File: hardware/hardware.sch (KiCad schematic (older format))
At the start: 98 parts, among them J1 DB25_Female, J2 USB_B_Micro, J3 RJ45_Bel_SI-60062-F-68net, U1 MIC5319, U11 ENC28J60x-SO, U12 74LVC14, U2 74LVTH126, U3 74LVTH126, U4 LM1117-ADJ, U5 74LVTH126, U6 74LVTH126, U7 STM32F072R8Tx, U8 74LVC245, Y1 8MHz, Y2 25MHz

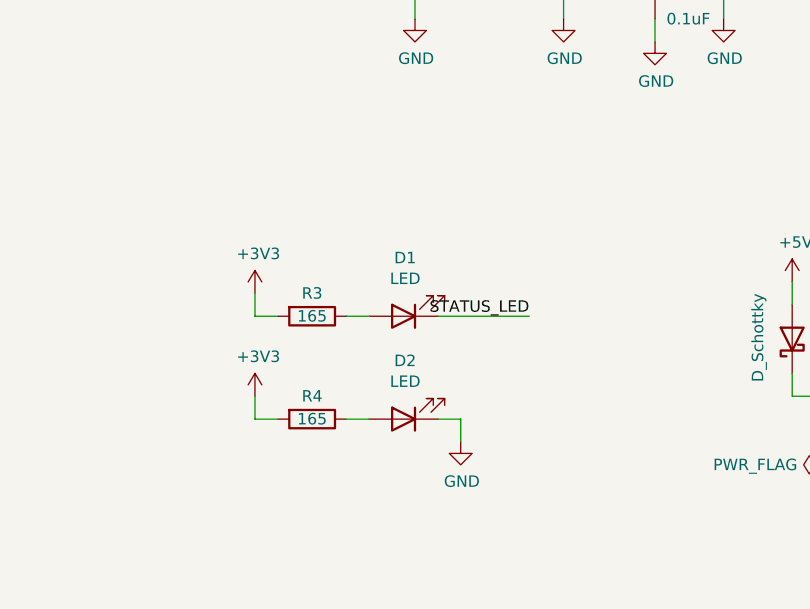
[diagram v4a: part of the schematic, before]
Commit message: feat: add connectors for external LEDs
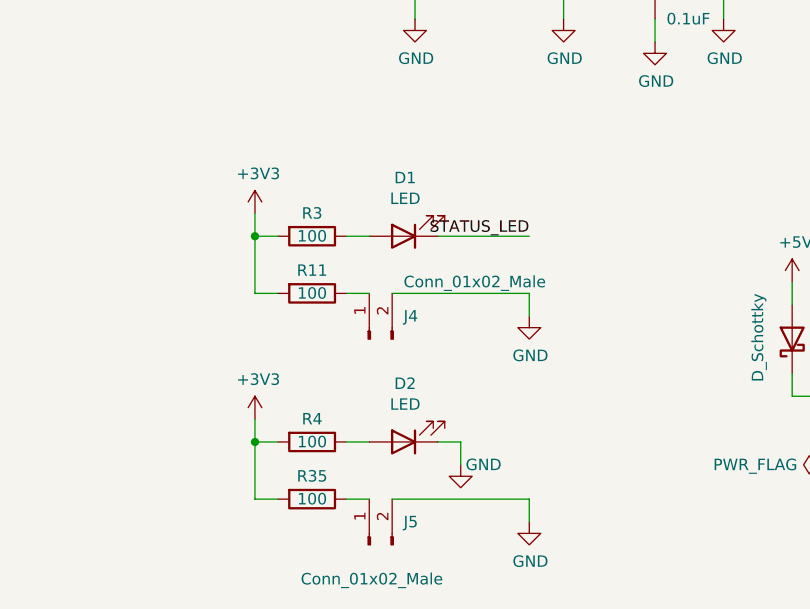
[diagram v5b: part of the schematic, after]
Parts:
- added J4, J5: Conn_01x02_Male, Connector_PinHeader_2.54mm:PinHeader_1x02_P2.54mm_Vertical, symbol Connector:Conn_01x02_Male
- added R11, R35: 100, Resistor_SMD:R_0805_2012Metric_Pad1.15x1.40mm_HandSolder, symbol Device:R
- J1: footprint kicad-footprints-perso:D25S13A -> kicad-footprints-perso:DSUB-25_Female_Horizontal_Double
- R3, R4: value 165 -> 100
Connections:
- net +3V3: now also R11.2, R35.2
- net GND: now also J4.2 (Pin_2), J5.2 (Pin_2)
- new net: J4.1 (Pin_1), R11.1
- new net: J5.1 (Pin_1), R35.1
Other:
- moved on the sheet: D1, D2, R3, R4
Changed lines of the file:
@@
 $EndComp
 Wire Wire Line
-	1000 10250 1000 10350
-Wire Wire Line
-	1000 10350 1100 10350
-Wire Wire Line
-	1400 10350 1500 10350
-Wire Wire Line
-	1800 10350 1900 10350
-Wire Wire Line
-	1900 10350 1900 10450
+	1000 10350 1000 10450
+Wire Wire Line
+	1000 10450 1100 10450
+Wire Wire Line
+	1400 10450 1500 10450
+Wire Wire Line
+	1800 10450 1900 10450
+Wire Wire Line
+	1900 10450 1900 10550
 $Comp
 L power:GND #PWR?
 U 1 1 6030DBBA
-P 1900 10450
-F 0 "#PWR?" H 1900 10200 50  0001 C CNN
-F 1 "GND" H 1905 10277 50  0000 C CNN
-F 2 "" H 1900 10450 50  0001 C CNN
-F 3 "" H 1900 10450 50  0001 C CNN
-	1    1900 10450
-	1    0    0    -1
-$EndComp
-Wire Wire Line
-	1000 9800 1000 9900
-Wire Wire Line
-	1000 9900 1100 9900
+P 1900 10550
+F 0 "#PWR?" H 1900 10300 50  0001 C CNN
+F 1 "GND" H 2000 10550 50  0000 C CNN
+F 2 "" H 1900 10550 50  0001 C CNN
+F 3 "" H 1900 10550 50  0001 C CNN
+	1    1900 10550
+	1    0    0    -1
+$EndComp
+Wire Wire Line
+	1000 9450 1000 9550
+Wire Wire Line
+	1000 9550 1100 9550
 $Comp
 L power:+3V3 #PWR?
 U 1 1 6032DBF1
-P 1000 9800
-F 0 "#PWR?" H 1000 9650 50  0001 C CNN
-F 1 "+3V3" H 1015 9973 50  0000 C CNN
-F 2 "" H 1000 9800 50  0001 C CNN
-F 3 "" H 1000 9800 50  0001 C CNN
-	1    1000 9800
-	1    0    0    -1
-$EndComp
-Wire Wire Line
-	1400 9900 1500 9900
-Wire Wire Line
-	1800 9900 2200 9900
-Text Label 2200 9900 2    50   ~ 0
+P 1000 9450
+F 0 "#PWR?" H 1000 9300 50  0001 C CNN
+F 1 "+3V3" H 1015 9623 50  0000 C CNN
+F 2 "" H 1000 9450 50  0001 C CNN
+F 3 "" H 1000 9450 50  0001 C CNN
+	1    1000 9450
+	1    0    0    -1
+$EndComp
+Wire Wire Line
+	1400 9550 1500 9550
+Wire Wire Line
+	1800 9550 2200 9550
+Text Label 2200 9550 2    50   ~ 0
 STATUS_LED
 NoConn ~ 12300 8400
@@
 L Device:LED D1
 U 1 1 6034F780
-P 1650 9900
-F 0 "D1" H 1643 9645 50  0000 C CNN
-F 1 "LED" H 1643 9736 50  0000 C CNN
-F 2 "LED_SMD:LED_1206_3216Metric_Pad1.42x1.75mm_HandSolder" H 1650 9900 50  0001 C CNN
-F 3 "~" H 1650 9900 50  0001 C CNN
-F 4 "60-1456-1-ND" H 1650 9900 50  0001 C CNN "Digi-Key_PN"
-	1    1650 9900
+P 1650 9550
+F 0 "D1" H 1643 9295 50  0000 C CNN
+F 1 "LED" H 1643 9386 50  0000 C CNN
+F 2 "LED_SMD:LED_1206_3216Metric_Pad1.42x1.75mm_HandSolder" H 1650 9550 50  0001 C CNN
+F 3 "~" H 1650 9550 50  0001 C CNN
+F 4 "60-1456-1-ND" H 1650 9550 50  0001 C CNN "Digi-Key_PN"
+	1    1650 9550
 	-1   0    0    1
 $EndComp
@@
 L Device:R R3
 U 1 1 6032EE5C
-P 1250 9900
-F 0 "R3" V 1150 9900 50  0000 C CNN
-F 1 "165" V 1250 9900 50  0000 C CNN
-F 2 "Resistor_SMD:R_0805_2012Metric_Pad1.15x1.40mm_HandSolder" V 1180 9900 50  0001 C CNN
-F 3 "~" H 1250 9900 50  0001 C CNN
-F 4 "RMCF0805FT165RCT-ND" H 1250 9900 50  0001 C CNN "Digi-Key_PN"
-	1    1250 9900
+P 1250 9550
+F 0 "R3" V 1150 9550 50  0000 C CNN
+F 1 "100" V 1250 9550 50  0000 C CNN
+F 2 "Resistor_SMD:R_0805_2012Metric_Pad1.15x1.40mm_HandSolder" V 1180 9550 50  0001 C CNN
+F 3 "~" H 1250 9550 50  0001 C CNN
+F 4 "RMCF0805FT165RCT-ND" H 1250 9550 50  0001 C CNN "Digi-Key_PN"
+	1    1250 9550
 	0    1    1    0
 $EndComp
@@
 L Device:LED D2
 U 1 1 602EDF34
-P 1650 10350
-F 0 "D2" H 1643 10095 50  0000 C CNN
-F 1 "LED" H 1643 10186 50  0000 C CNN
-F 2 "LED_SMD:LED_1206_3216Metric_Pad1.42x1.75mm_HandSolder" H 1650 10350 50  0001 C CNN
-F 3 "~" H 1650 10350 50  0001 C CNN
-F 4 "60-1456-1-ND" H 1650 10350 50  0001 C CNN "Digi-Key_PN"
-	1    1650 10350
+P 1650 10450
+F 0 "D2" H 1643 10195 50  0000 C CNN
+F 1 "LED" H 1643 10286 50  0000 C CNN
+F 2 "LED_SMD:LED_1206_3216Metric_Pad1.42x1.75mm_HandSolder" H 1650 10450 50  0001 C CNN
+F 3 "~" H 1650 10450 50  0001 C CNN
+F 4 "60-1456-1-ND" H 1650 10450 50  0001 C CNN "Digi-Key_PN"
+	1    1650 10450
 	-1   0    0    1
 $EndComp
@@
 L Device:R R4
 U 1 1 602CE979
-P 1250 10350
-F 0 "R4" V 1150 10350 50  0000 C CNN
-F 1 "165" V 1250 10350 50  0000 C CNN
-F 2 "Resistor_SMD:R_0805_2012Metric_Pad1.15x1.40mm_HandSolder" V 1180 10350 50  0001 C CNN
-F 3 "~" H 1250 10350 50  0001 C CNN
-F 4 "RMCF0805FT165RCT-ND" H 1250 10350 50  0001 C CNN "Digi-Key_PN"
-	1    1250 10350
+P 1250 10450
+F 0 "R4" V 1150 10450 50  0000 C CNN
+F 1 "100" V 1250 10450 50  0000 C CNN
+F 2 "Resistor_SMD:R_0805_2012Metric_Pad1.15x1.40mm_HandSolder" V 1180 10450 50  0001 C CNN
+F 3 "~" H 1250 10450 50  0001 C CNN
+F 4 "RMCF0805FT165RCT-ND" H 1250 10450 50  0001 C CNN "Digi-Key_PN"
+	1    1250 10450
 	0    1    1    0
 $EndComp
@@
 F 0 "J1" H 15430 2096 50  0000 L CNN
 F 1 "DB25_Female" H 15430 2005 50  0000 L CNN
-F 2 "kicad-footprints-perso:D25S13A" H 15250 2050 50  0001 C CNN
+F 2 "kicad-footprints-perso:DSUB-25_Female_Horizontal_Double" H 15250 2050 50  0001 C CNN
 F 3 " ~" H 15250 2050 50  0001 C CNN
 F 4 "609-1507-ND" H 15250 2050 50  0001 C CNN "Digi-Key_PN"
@@
 L power:+3V3 #PWR?
 U 1 1 603F481A
-P 1000 10250
-F 0 "#PWR?" H 1000 10100 50  0001 C CNN
-F 1 "+3V3" H 1015 10423 50  0000 C CNN
-F 2 "" H 1000 10250 50  0001 C CNN
-F 3 "" H 1000 10250 50  0001 C CNN
-	1    1000 10250
+P 1000 10350
+F 0 "#PWR?" H 1000 10200 50  0001 C CNN
+F 1 "+3V3" H 1015 10523 50  0000 C CNN
+F 2 "" H 1000 10350 50  0001 C CNN
+F 3 "" H 1000 10350 50  0001 C CNN
+	1    1000 10350
 	1    0    0    -1
 $EndComp
@@
 	1    0    0    -1
 $EndComp
+Wire Wire Line
+	1000 9800 1100 9800
+Wire Wire Line
+	1400 9800 1500 9800
+$Comp
+L Device:R R11
+U 1 1 6118A7D0
+P 1250 9800
+F 0 "R11" V 1150 9800 50  0000 C CNN
+F 1 "100" V 1250 9800 50  0000 C CNN
+F 2 "Resistor_SMD:R_0805_2012Metric_Pad1.15x1.40mm_HandSolder" V 1180 9800 50  0001 C CNN
+F 3 "~" H 1250 9800 50  0001 C CNN
+F 4 "RMCF0805FT165RCT-ND" H 1250 9800 50  0001 C CNN "Digi-Key_PN"
+	1    1250 9800
+	0    1    1    0
+$EndComp
+Wire Wire Line
+	1000 9550 1000 9800
+Connection ~ 1000 9550
+$Comp
+L Connector:Conn_01x02_Male J4
+U 1 1 61266EA3
+P 1500 10000
+F 0 "J4" V 1600 9850 50  0000 R CNN
+F 1 "Conn_01x02_Male" V 1750 9850 50  0000 R CNN
+F 2 "Connector_PinHeader_2.54mm:PinHeader_1x02_P2.54mm_Vertical" H 1500 10000 50  0001 C CNN
+F 3 "~" H 1500 10000 50  0001 C CNN
+	1    1500 10000
+	0    -1   -1   0
+$EndComp
+Wire Wire Line
+	1600 9800 2200 9800
+Wire Wire Line
+	2200 9800 2200 9900
+$Comp
+L power:GND #PWR?
+U 1 1 612D7C08
+P 2200 9900
+F 0 "#PWR?" H 2200 9650 50  0001 C CNN
+F 1 "GND" H 2205 9727 50  0000 C CNN
+F 2 "" H 2200 9900 50  0001 C CNN
+F 3 "" H 2200 9900 50  0001 C CNN
+	1    2200 9900
+	1    0    0    -1
+$EndComp
+Wire Wire Line
+	1000 10700 1100 10700
+Wire Wire Line
+	1400 10700 1500 10700
+$Comp
+L Device:R R35
+U 1 1 612D9E8B
+P 1250 10700
+F 0 "R35" V 1150 10700 50  0000 C CNN
+F 1 "100" V 1250 10700 50  0000 C CNN
+F 2 "Resistor_SMD:R_0805_2012Metric_Pad1.15x1.40mm_HandSolder" V 1180 10700 50  0001 C CNN
+F 3 "~" H 1250 10700 50  0001 C CNN
+F 4 "RMCF0805FT165RCT-ND" H 1250 10700 50  0001 C CNN "Digi-Key_PN"
+	1    1250 10700
+	0    1    1    0
+$EndComp
+Wire Wire Line
+	1000 10450 1000 10700
+$Comp
+L Connector:Conn_01x02_Male J5
+U 1 1 612D9E92
+P 1500 10900
+F 0 "J5" V 1600 10750 50  0000 R CNN
+F 1 "Conn_01x02_Male" V 1350 11200 50  0000 R CNN
+F 2 "Connector_PinHeader_2.54mm:PinHeader_1x02_P2.54mm_Vertical" H 1500 10900 50  0001 C CNN
+F 3 "~" H 1500 10900 50  0001 C CNN
+	1    1500 10900
+	0    -1   -1   0
+$EndComp
+Wire Wire Line
+	1600 10700 2200 10700
+Wire Wire Line
+	2200 10700 2200 10800
+$Comp
+L power:GND #PWR?
+U 1 1 612D9E9A
+P 2200 10800
+F 0 "#PWR?" H 2200 10550 50  0001 C CNN
+F 1 "GND" H 2205 10627 50  0000 C CNN
+F 2 "" H 2200 10800 50  0001 C CNN
+F 3 "" H 2200 10800 50  0001 C CNN
+	1    2200 10800
+	1    0    0    -1
+$EndComp
+Connection ~ 1000 10450
 $EndSCHEMATC

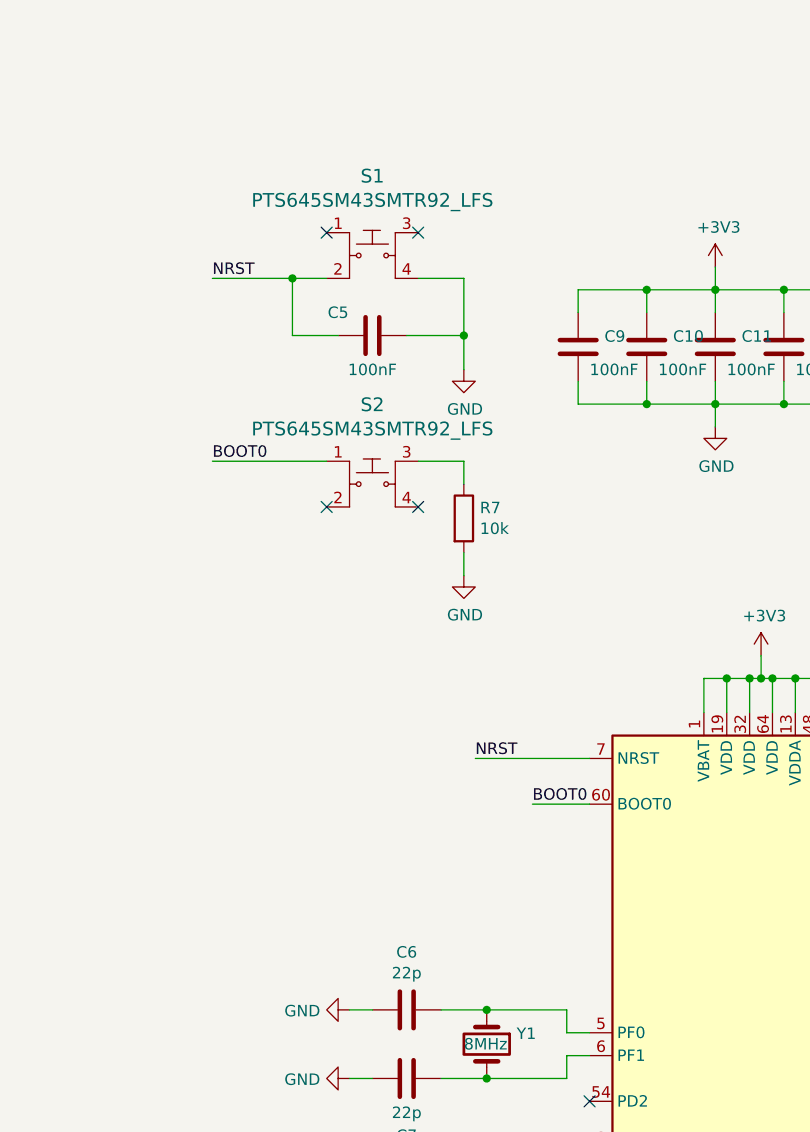
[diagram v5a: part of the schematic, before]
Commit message: fix: boot and rst signal badly pulled up/down
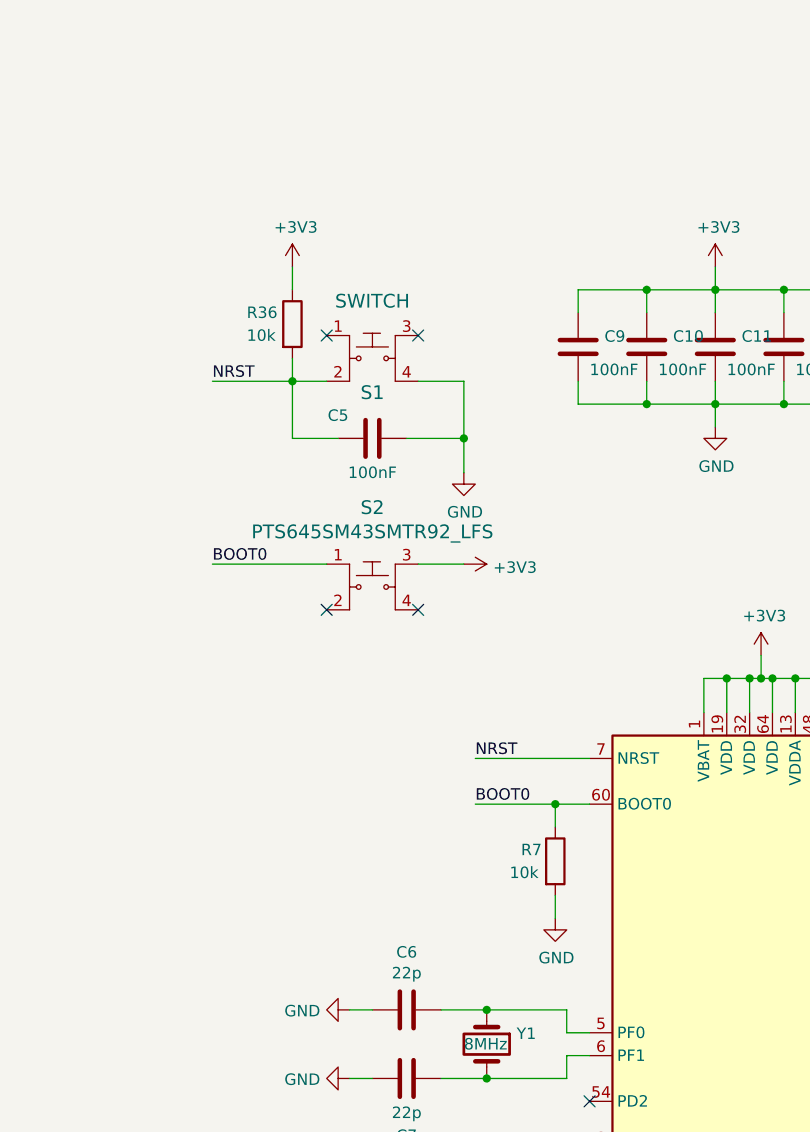
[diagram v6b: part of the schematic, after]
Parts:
- added R36: 10k, Resistor_SMD:R_0805_2012Metric_Pad1.15x1.40mm_HandSolder, symbol Device:R
- S1: value PTS645SM43SMTR92_LFS -> SWITCH
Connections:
- net +3V3: now also S2.3, R36.1
- net BOOT0: now also R7.1
- net NRST: now also R36.2
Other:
- moved on the sheet: C5, R7, S1, S2
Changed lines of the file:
@@
 NRST
 Wire Wire Line
-	1550 900  1750 900
-Wire Wire Line
-	1750 900  1750 1150
-Wire Wire Line
-	1500 1150 1750 1150
-Connection ~ 1750 1150
-Wire Wire Line
-	1750 1150 1750 1300
-Wire Wire Line
-	1200 1150 1000 1150
-Wire Wire Line
-	1000 1150 1000 900
-Connection ~ 1000 900
-Wire Wire Line
-	1000 900  1150 900
+	1550 1350 1750 1350
+Wire Wire Line
+	1750 1350 1750 1600
+Wire Wire Line
+	1500 1600 1750 1600
+Connection ~ 1750 1600
+Wire Wire Line
+	1750 1600 1750 1750
+Wire Wire Line
+	1200 1600 1000 1600
+Wire Wire Line
+	1000 1600 1000 1350
+Connection ~ 1000 1350
+Wire Wire Line
+	1000 1350 1150 1350
 $Comp
 L power:GND #PWR?
 U 1 1 6108C520
-P 1750 1300
-F 0 "#PWR?" H 1750 1050 50  0001 C CNN
-F 1 "GND" H 1755 1127 50  0000 C CNN
-F 2 "" H 1750 1300 50  0001 C CNN
-F 3 "" H 1750 1300 50  0001 C CNN
-	1    1750 1300
-	1    0    0    -1
-$EndComp
-Wire Wire Line
-	650  900  1000 900
-Text Label 650  900  0    50   ~ 0
+P 1750 1750
+F 0 "#PWR?" H 1750 1500 50  0001 C CNN
+F 1 "GND" H 1755 1577 50  0000 C CNN
+F 2 "" H 1750 1750 50  0001 C CNN
+F 3 "" H 1750 1750 50  0001 C CNN
+	1    1750 1750
+	1    0    0    -1
+$EndComp
+Wire Wire Line
+	650  1350 1000 1350
+Text Label 650  1350 0    50   ~ 0
 NRST
 Wire Wire Line
-	650  1700 1150 1700
-Wire Wire Line
-	1550 1700 1750 1700
-Wire Wire Line
-	1750 1700 1750 1800
-Wire Wire Line
-	1750 2100 1750 2200
-$Comp
-L power:GND #PWR?
-U 1 1 611B4FDC
-P 1750 2200
-F 0 "#PWR?" H 1750 1950 50  0001 C CNN
-F 1 "GND" H 1755 2027 50  0000 C CNN
-F 2 "" H 1750 2200 50  0001 C CNN
-F 3 "" H 1750 2200 50  0001 C CNN
-	1    1750 2200
-	1    0    0    -1
-$EndComp
-Text Label 650  1700 0    50   ~ 0
-BOOT0
-Wire Wire Line
-	2300 3200 2050 3200
-Text Label 2050 3200 0    50   ~ 0
+	1550 2150 1750 2150
+Text Label 650  2150 0    50   ~ 0
 BOOT0
 Wire Wire Line
@@
 Wire Wire Line
 	5650 3400 5900 3400
-NoConn ~ 1150 700
-NoConn ~ 1550 700
-NoConn ~ 1150 1900
-NoConn ~ 1550 1900
+NoConn ~ 1150 1150
+NoConn ~ 1550 1150
+NoConn ~ 1150 2350
+NoConn ~ 1550 2350
 $Comp
 L 68net:USB_B_Micro J2
@@
 L dk_Tactile-Switches:PTS645SM43SMTR92_LFS S1
 U 1 1 63523958
-P 1350 800
-F 0 "S1" H 1350 1147 60  0000 C CNN
-F 1 "PTS645SM43SMTR92_LFS" H 1350 1041 60  0000 C CNN
-F 2 "digikey-footprints:Switch_Tactile_SMD_6x6mm" H 1550 1000 60  0001 L CNN
-F 3 "https://www.ckswitches.com/media/1471/pts645.pdf" H 1550 1100 60  0001 L CNN
-F 4 "TL3301AF160QG" H 1550 1200 60  0001 L CNN "Digi-Key_PN"
-F 5 "" H 1550 1300 60  0001 L CNN "MPN"
-F 6 "Switches" H 1550 1400 60  0001 L CNN "Category"
-F 7 "Tactile Switches" H 1550 1500 60  0001 L CNN "Family"
-F 8 "" H 1550 1600 60  0001 L CNN "DK_Datasheet_Link"
-F 9 "" H 1550 1700 60  0001 L CNN "DK_Detail_Page"
-F 10 "" H 1550 1800 60  0001 L CNN "Description"
-F 11 "C&K" H 1550 1900 60  0001 L CNN "Manufacturer"
-F 12 "Active" H 1550 2000 60  0001 L CNN "Status"
-	1    1350 800
+P 1350 1250
+F 0 "S1" H 1350 1100 60  0000 C CNN
+F 1 "SWITCH" H 1350 1500 60  0000 C CNN
+F 2 "digikey-footprints:Switch_Tactile_SMD_6x6mm" H 1550 1450 60  0001 L CNN
+F 3 "https://www.ckswitches.com/media/1471/pts645.pdf" H 1550 1550 60  0001 L CNN
+F 4 "TL3301AF160QG" H 1550 1650 60  0001 L CNN "Digi-Key_PN"
+F 5 "" H 1550 1750 60  0001 L CNN "MPN"
+F 6 "Switches" H 1550 1850 60  0001 L CNN "Category"
+F 7 "Tactile Switches" H 1550 1950 60  0001 L CNN "Family"
+F 8 "" H 1550 2050 60  0001 L CNN "DK_Datasheet_Link"
+F 9 "" H 1550 2150 60  0001 L CNN "DK_Detail_Page"
+F 10 "" H 1550 2250 60  0001 L CNN "Description"
+F 11 "C&K" H 1550 2350 60  0001 L CNN "Manufacturer"
+F 12 "Active" H 1550 2450 60  0001 L CNN "Status"
+	1    1350 1250
 	1    0    0    -1
 $EndComp
@@
 L dk_Tactile-Switches:PTS645SM43SMTR92_LFS S2
 U 1 1 635217E4
-P 1350 1800
-F 0 "S2" H 1350 2147 60  0000 C CNN
-F 1 "PTS645SM43SMTR92_LFS" H 1350 2041 60  0000 C CNN
-F 2 "digikey-footprints:Switch_Tactile_SMD_6x6mm" H 1550 2000 60  0001 L CNN
-F 3 "https://www.ckswitches.com/media/1471/pts645.pdf" H 1550 2100 60  0001 L CNN
-F 4 "TL3301AF160QG" H 1550 2200 60  0001 L CNN "Digi-Key_PN"
-F 5 "" H 1550 2300 60  0001 L CNN "MPN"
-F 6 "Switches" H 1550 2400 60  0001 L CNN "Category"
-F 7 "Tactile Switches" H 1550 2500 60  0001 L CNN "Family"
-F 8 "" H 1550 2600 60  0001 L CNN "DK_Datasheet_Link"
-F 9 "" H 1550 2700 60  0001 L CNN "DK_Detail_Page"
-F 10 "" H 1550 2800 60  0001 L CNN "Description"
-F 11 "C&K" H 1550 2900 60  0001 L CNN "Manufacturer"
-F 12 "Active" H 1550 3000 60  0001 L CNN "Status"
-	1    1350 1800
+P 1350 2250
+F 0 "S2" H 1350 2597 60  0000 C CNN
+F 1 "PTS645SM43SMTR92_LFS" H 1350 2491 60  0000 C CNN
+F 2 "digikey-footprints:Switch_Tactile_SMD_6x6mm" H 1550 2450 60  0001 L CNN
+F 3 "https://www.ckswitches.com/media/1471/pts645.pdf" H 1550 2550 60  0001 L CNN
+F 4 "TL3301AF160QG" H 1550 2650 60  0001 L CNN "Digi-Key_PN"
+F 5 "" H 1550 2750 60  0001 L CNN "MPN"
+F 6 "Switches" H 1550 2850 60  0001 L CNN "Category"
+F 7 "Tactile Switches" H 1550 2950 60  0001 L CNN "Family"
+F 8 "" H 1550 3050 60  0001 L CNN "DK_Datasheet_Link"
+F 9 "" H 1550 3150 60  0001 L CNN "DK_Detail_Page"
+F 10 "" H 1550 3250 60  0001 L CNN "Description"
+F 11 "C&K" H 1550 3350 60  0001 L CNN "Manufacturer"
+F 12 "Active" H 1550 3450 60  0001 L CNN "Status"
+	1    1350 2250
 	1    0    0    -1
 $EndComp
@@
 $EndComp
 $Comp
-L Device:R R7
-U 1 1 611792DD
-P 1750 1950
-F 0 "R7" H 1820 1996 50  0000 L CNN
-F 1 "10k" H 1820 1905 50  0000 L CNN
-F 2 "Resistor_SMD:R_0805_2012Metric_Pad1.15x1.40mm_HandSolder" V 1680 1950 50  0001 C CNN
-F 3 "~" H 1750 1950 50  0001 C CNN
-F 4 "RMCF0603JT10K0CT-ND" H 1750 1950 50  0001 C CNN "Digi-Key_PN"
-	1    1750 1950
-	1    0    0    -1
-$EndComp
-$Comp
 L Device:C C5
 U 1 1 61019897
-P 1350 1150
-F 0 "C5" V 1250 1000 50  0000 C CNN
-F 1 "100nF" V 1500 1150 50  0000 C CNN
-F 2 "Capacitor_SMD:C_1206_3216Metric_Pad1.42x1.75mm_HandSolder" H 1388 1000 50  0001 C CNN
-F 3 "~" H 1350 1150 50  0001 C CNN
-F 4 "1276-1017-1-ND" H 1350 1150 50  0001 C CNN "Digi-Key_PN"
-	1    1350 1150
+P 1350 1600
+F 0 "C5" V 1250 1450 50  0000 C CNN
+F 1 "100nF" V 1500 1600 50  0000 C CNN
+F 2 "Capacitor_SMD:C_1206_3216Metric_Pad1.42x1.75mm_HandSolder" H 1388 1450 50  0001 C CNN
+F 3 "~" H 1350 1600 50  0001 C CNN
+F 4 "1276-1017-1-ND" H 1350 1600 50  0001 C CNN "Digi-Key_PN"
+	1    1350 1600
 	0    1    1    0
 $EndComp
@@
 $EndComp
 Connection ~ 1000 10450
+$Comp
+L power:+3V3 #PWR?
+U 1 1 5FBC85D1
+P 1750 2150
+F 0 "#PWR?" H 1750 2000 50  0001 C CNN
+F 1 "+3V3" V 1765 2278 50  0000 L CNN
+F 2 "" H 1750 2150 50  0001 C CNN
+F 3 "" H 1750 2150 50  0001 C CNN
+	1    1750 2150
+	0    1    1    0
+$EndComp
+Wire Wire Line
+	650  2150 1150 2150
+Wire Wire Line
+	1000 850  1000 950
+Wire Wire Line
+	1000 1250 1000 1350
+$Comp
+L Device:R R36
+U 1 1 5FC40257
+P 1000 1100
+F 0 "R36" H 800 1150 50  0000 L CNN
+F 1 "10k" H 800 1050 50  0000 L CNN
+F 2 "Resistor_SMD:R_0805_2012Metric_Pad1.15x1.40mm_HandSolder" V 930 1100 50  0001 C CNN
+F 3 "~" H 1000 1100 50  0001 C CNN
+F 4 "RMCF0603JT10K0CT-ND" H 1000 1100 50  0001 C CNN "Digi-Key_PN"
+	1    1000 1100
+	1    0    0    -1
+$EndComp
+$Comp
+L power:+3V3 #PWR?
+U 1 1 5FD23831
+P 1000 850
+F 0 "#PWR?" H 1000 700 50  0001 C CNN
+F 1 "+3V3" H 1015 1023 50  0000 C CNN
+F 2 "" H 1000 850 50  0001 C CNN
+F 3 "" H 1000 850 50  0001 C CNN
+	1    1000 850
+	1    0    0    -1
+$EndComp
+Wire Wire Line
+	2300 3200 2150 3200
+Connection ~ 2150 3200
+Wire Wire Line
+	2150 3200 2150 3300
+$Comp
+L power:GND #PWR?
+U 1 1 611B4FDC
+P 2150 3700
+F 0 "#PWR?" H 2150 3450 50  0001 C CNN
+F 1 "GND" H 2155 3527 50  0000 C CNN
+F 2 "" H 2150 3700 50  0001 C CNN
+F 3 "" H 2150 3700 50  0001 C CNN
+	1    2150 3700
+	1    0    0    -1
+$EndComp
+Wire Wire Line
+	2150 3600 2150 3700
+$Comp
+L Device:R R7
+U 1 1 611792DD
+P 2150 3450
+F 0 "R7" H 2000 3500 50  0000 L CNN
+F 1 "10k" H 1950 3400 50  0000 L CNN
+F 2 "Resistor_SMD:R_0805_2012Metric_Pad1.15x1.40mm_HandSolder" V 2080 3450 50  0001 C CNN
+F 3 "~" H 2150 3450 50  0001 C CNN
+F 4 "RMCF0603JT10K0CT-ND" H 2150 3450 50  0001 C CNN "Digi-Key_PN"
+	1    2150 3450
+	1    0    0    -1
+$EndComp
+Text Label 1800 3200 0    50   ~ 0
+BOOT0
+Wire Wire Line
+	1800 3200 2150 3200
 $EndSCHEMATC
